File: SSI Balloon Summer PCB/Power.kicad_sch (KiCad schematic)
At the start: 25 parts, among them J1 Conn_01x02, Q2 DMG2305UX-7, SW1 SW_SPDT, U2 TPS63070RNMR, U3 AP2112K-3.3TRG1, U4 XC6206P182MR-sot23

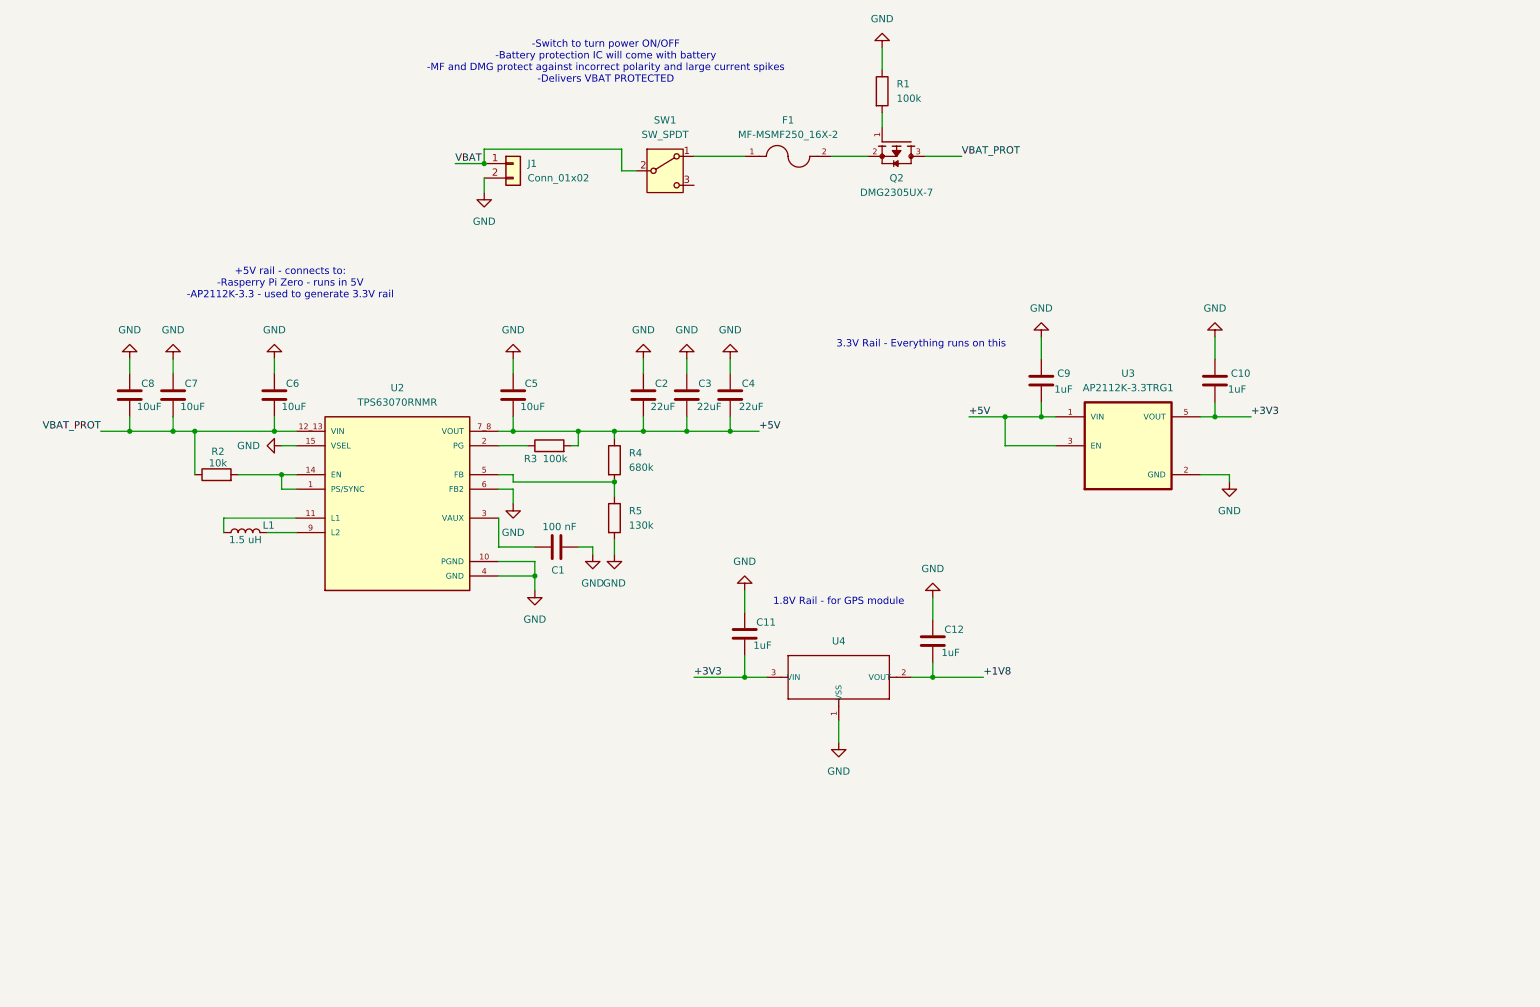
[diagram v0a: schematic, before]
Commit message: Worked on LoRa and APRS
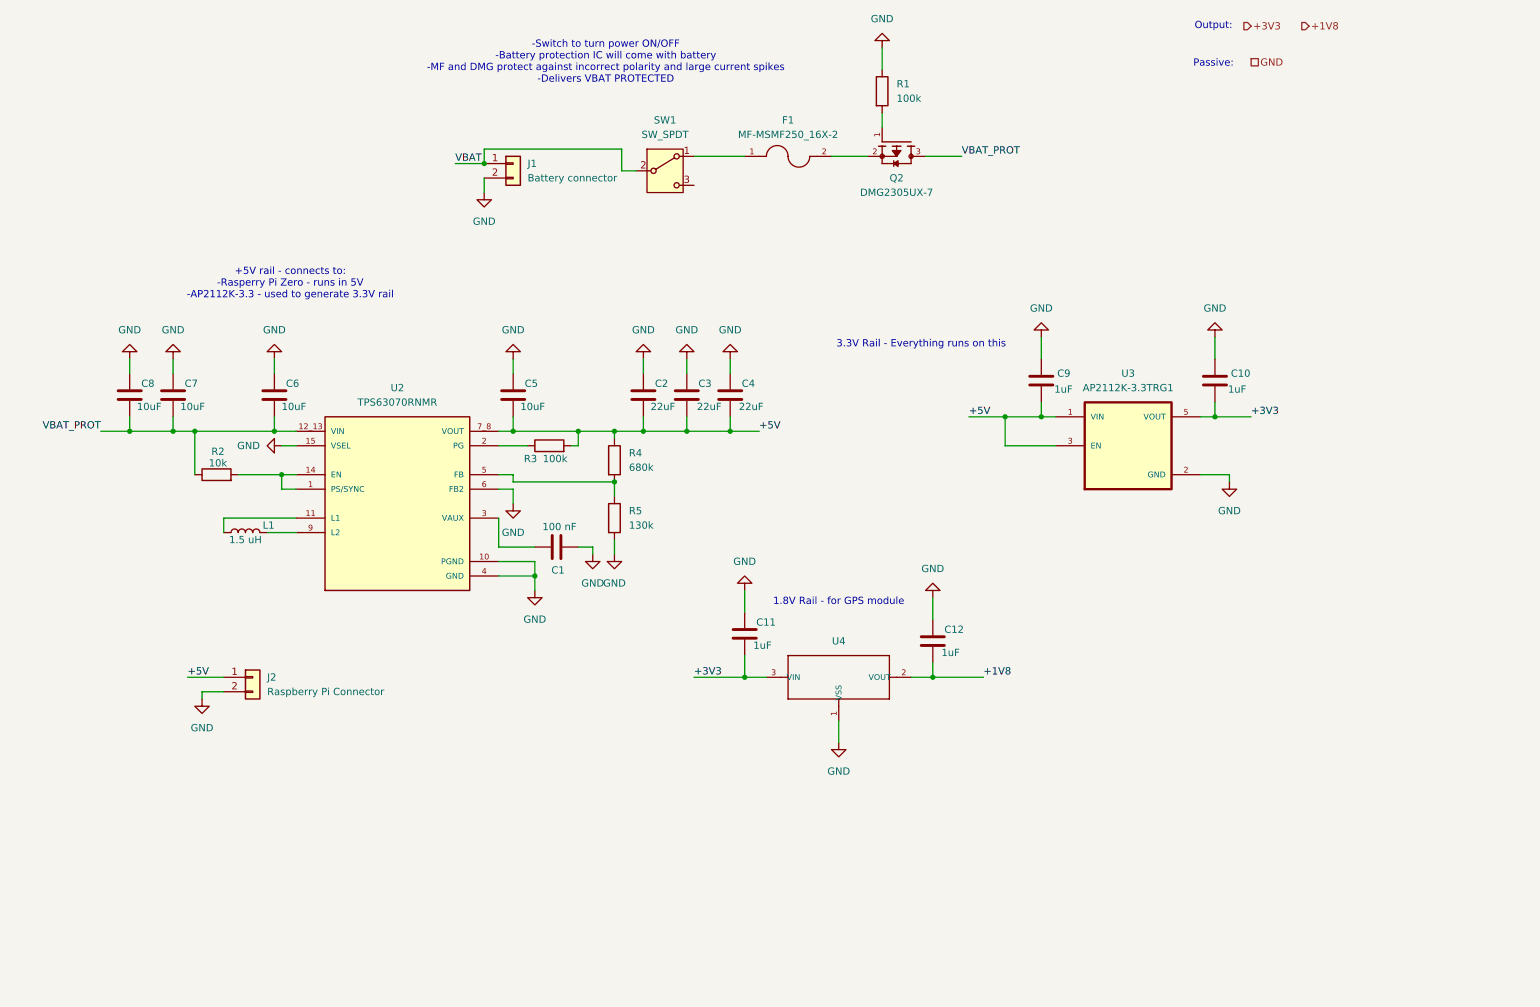
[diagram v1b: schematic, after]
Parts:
- added J2: Raspberry Pi Connector, symbol Connector_Generic:Conn_01x02
- J1: value Conn_01x02 -> Battery connector
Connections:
- net +5V: now also J2.1 (Pin_1)
- net GND: now also J2.2 (Pin_2)
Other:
- note added: "Output:"
- note added: "Passive:"

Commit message: Added 4.1V rail for APRS
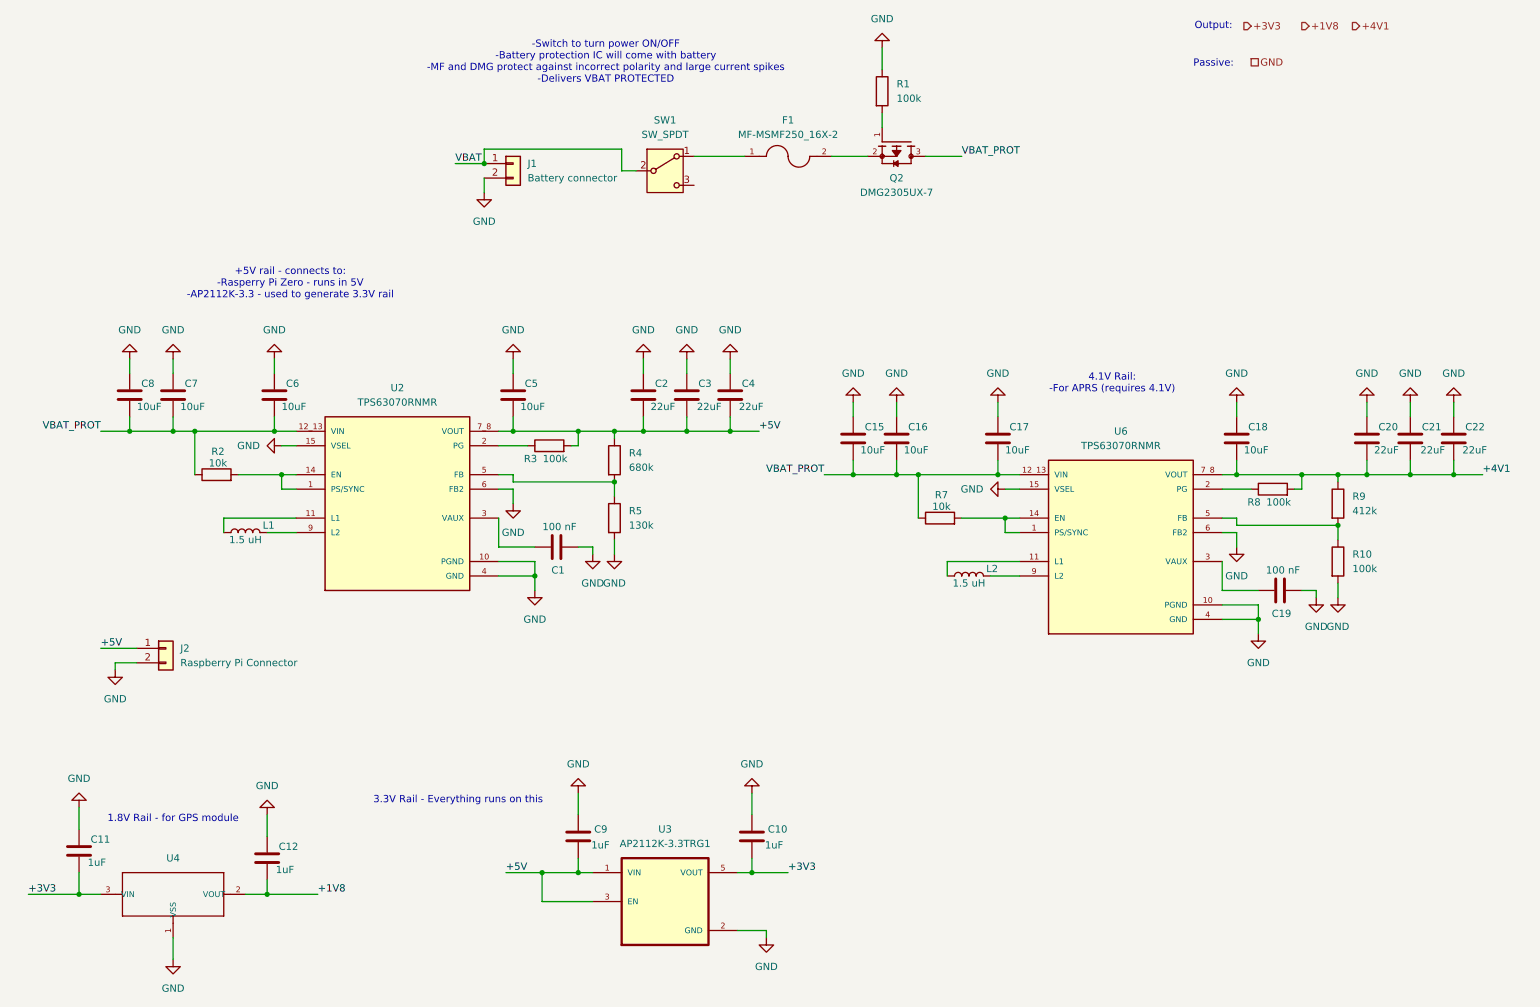
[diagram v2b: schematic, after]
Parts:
- added C15, C16, C17, C18: 10uF, symbol Device:C
- added C19: 100 nF, symbol Device:C
- added C20, C21, C22: 22uF, symbol Device:C
- added L2: 1.5 uH, symbol Device:L
- added R10, R8: 100k, symbol Device:R
- added R7: 10k, symbol Device:R
- added R9: 412k, symbol Device:R
- added U6: TPS63070RNMR, TPS63070RNMR:VREG_TPS63070RNMR, symbol TPS63070RNMR:TPS63070RNMR
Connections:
- net GND: now also C15.1, C16.1, C17.1, C18.1, C19.2, C20.1, C21.1, C22.1, R10.2, U6.10 (PGND), U6.15 (VSEL), U6.4 (GND), U6.6 (FB2)
- net VBAT_PROT: now also C15.2, C16.2, C17.2, R7.1, U6.12_13 (VIN)
- new net: R8.1, U6.2 (PG)
- new net: R10.1, R9.2, U6.5 (FB)
- new net: R7.2, U6.1 (PS/SYNC), U6.14 (EN)
- new net: L2.1, U6.11 (L1)
- new net: C19.1, U6.3 (VAUX)
- new net: L2.2, U6.9 (L2)
- new net +4V1: C18.2, C20.2, C21.2, C22.2, R8.2, R9.1, U6.7_8 (VOUT)
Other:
- note added: "4.1V Rail: -For APRS (requires 4.1V)"
- moved on the sheet: C10, C11, C12, C9, J2, U3, U4

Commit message: Standardized power symbols, added microSD sheet, and standardized hierarchical labels
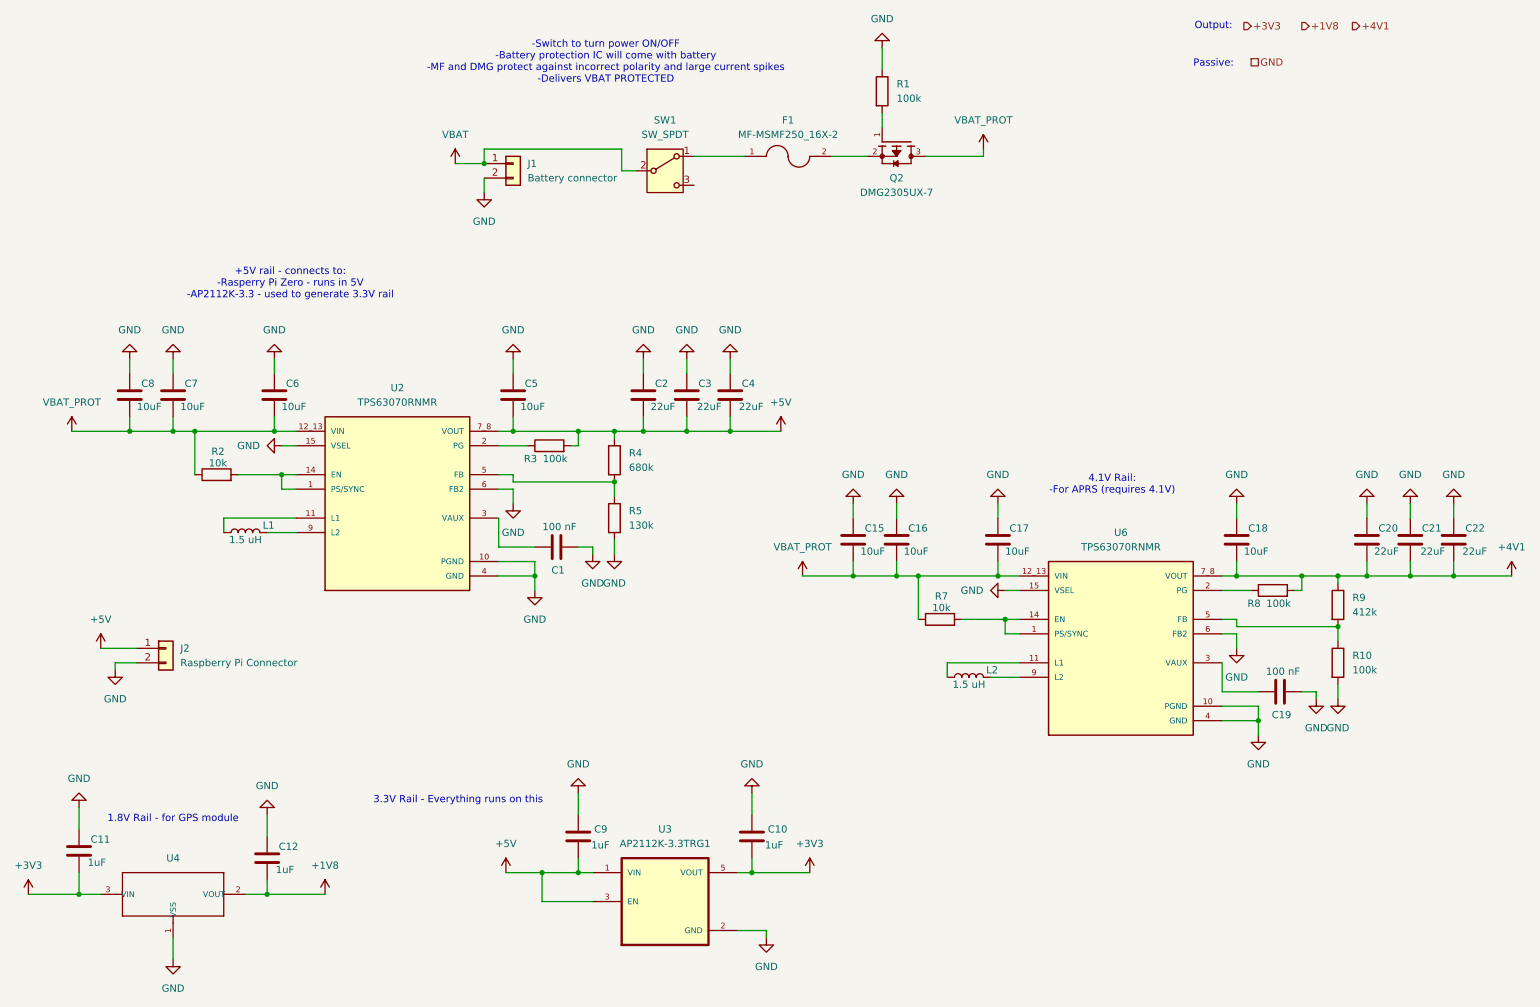
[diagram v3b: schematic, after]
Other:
- moved on the sheet: C15, C16, C17, C18, C19, C20, C21, C22, L2, R10, R7, R8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

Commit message: Finished GPS
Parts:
- removed C11, C12: 1uF, symbol Device:C
- removed U4: XC6206P182MR-sot23, PMIC-XC6206P182MR_SOT23_:SOT-23, symbol PMIC-XC6206P182MR_SOT23_:PMIC-XC6206P182MR_SOT23_
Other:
- note removed: "1.8V Rail - for GPS module"
